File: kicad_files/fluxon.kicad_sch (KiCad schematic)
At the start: 157 parts, among them J1 ARM SWD, J2 U-F-M5DD-W-2, J3 Conn_02x10, Q1 BSS138, Q2 MUN5335DW1T1G, SW1 ESC, SW10 O, SW11 P, SW12 DEL, SW13 TAB_125, SW14 A, SW15 S, SW16 D, SW17 F, SW18 G, SW19 H, SW2 Q, SW20 J, SW21 K, SW22 L, SW23 QUOTE, SW24 ENTER_175, SW25 LSHIFT_175, SW26 Z, SW27 X, SW28 C, SW29 V, SW3 W, SW30 B, SW31 N, SW32 M, SW33 COMMA, SW34 DOT, SW35 (D) RSHIFT_125, SW36 (D) FN_100, SW37 (F) RSHIFT_225, SW38 (I) RSHIFT_125, SW39 (I) SLASH_100, SW4 E, SW40 LCTRL_125, SW41 SUPER_100, SW42 LALT_100, SW43 SPC_625, SW44 RALT_125, SW45 RGUI_100, SW46 RCTRL_125, SW47 BKSP, SW48 BKSP_2U, SW49 PN_100, SW5 R, SW50 SPC_175, SW51 SPC_275, SW52 FN_100, SW53 RALT_100, SW54 LCTRL_150, SW55 LALT_150, SW56 SPC_700, SW57 RCTRL_150, SW58 RALT_150, SW6 T, SW7 Y, SW8 U, SW9 I, U1 USBLC6-2SC6, U2 MCP1700-3302E/TT, U3 STM32L072CBT6

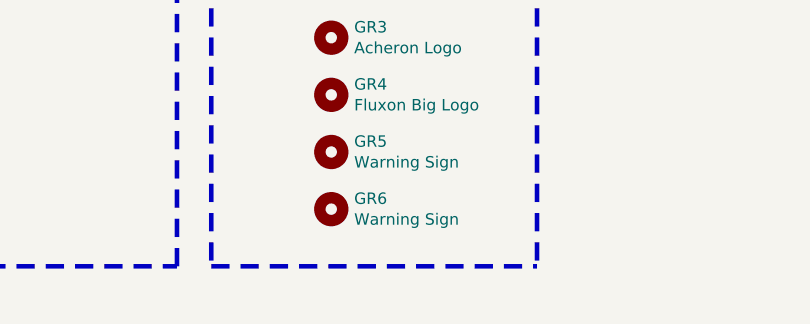
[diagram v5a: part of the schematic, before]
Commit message: Silkscreen and tracing improvements
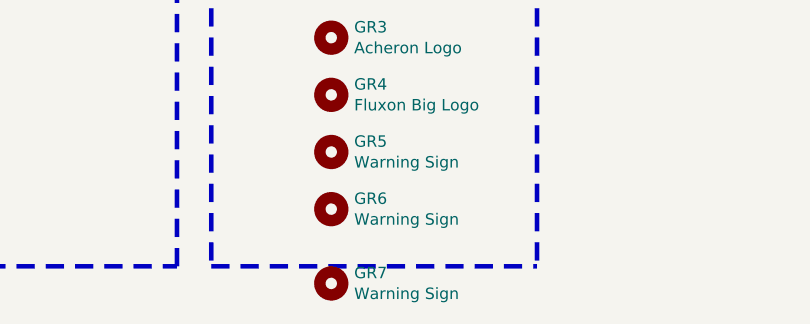
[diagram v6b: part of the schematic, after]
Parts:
- added GR7: Warning Sign, acheron_Graphics:warning_sign_3.6x3.2mm, symbol Mechanical:MountingHole
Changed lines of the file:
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@@
   (junction (at 518.16 250.825) (diameter 0) (color 0 0 0 0))
   (junction (at 518.16 257.175) (diameter 0) (color 0 0 0 0))
-  (no_connect (at 64.77 347.345))
   (no_connect (at 508.635 314.325))
+  (no_connect (at 64.77 347.345))
   (no_connect (at 123.19 267.335))
   (wire (pts (xy 41.275 265.43) (xy 45.085 265.43))
@@
   (symbol (lib_id "power:GND") (at 109.22 268.605 0) (mirror y) (unit 1)
     (in_bom yes) (on_board yes)
-    (property "Reference" "#PWR?" (id 0) (at 109.22 274.955 0)
+    (property "Reference" "#PWR0103" (id 0) (at 109.22 274.955 0)
       (effects (font (size 1.27 1.27)) hide)
     )
@@
     )
   )
+  (symbol (lib_id "Mechanical:MountingHole") (at 116.84 405.765 0) (unit 1)
+    (in_bom yes) (on_board yes)
+    (property "Reference" "GR7" (id 0) (at 119.38 404.5966 0)
+      (effects (font (size 1.27 1.27)) (justify left))
+    )
+    (property "Value" "Warning Sign" (id 1) (at 119.38 406.908 0)
+      (effects (font (size 1.27 1.27)) (justify left))
+    )
+    (property "Footprint" "acheron_Graphics:warning_sign_3.6x3.2mm" (id 2) (at 116.84 405.765 0)
+      (effects (font (size 1.27 1.27)) hide)
+    )
+    (property "Datasheet" "~" (id 3) (at 116.84 405.765 0)
+      (effects (font (size 1.27 1.27)) hide)
+    )
+  )
   (symbol (lib_id "Device:CP_Small") (at 133.985 325.755 0) (unit 1)
     (in_bom yes) (on_board yes)
@@
     )
     (path "/c38fbb2a-c35b-4672-8fd1-d78ffb85c184"
-      (reference "#PWR?") (unit 1)
+      (reference "#PWR0103") (unit 1)
     )
     (path "/d5072c79-7bfb-447b-9669-32e9fefbcb51"
@@
       (reference "GR6") (unit 1)
     )
+    (path "/6fded8dc-11a0-4d36-90ab-0545a8b854de"
+      (reference "GR7") (unit 1)
+    )
     (path "/3bf1228b-aee4-4155-9b64-00626b023658"
